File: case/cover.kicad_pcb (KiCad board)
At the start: 2 copper layers, 20.5 x 37 mm, 2 parts

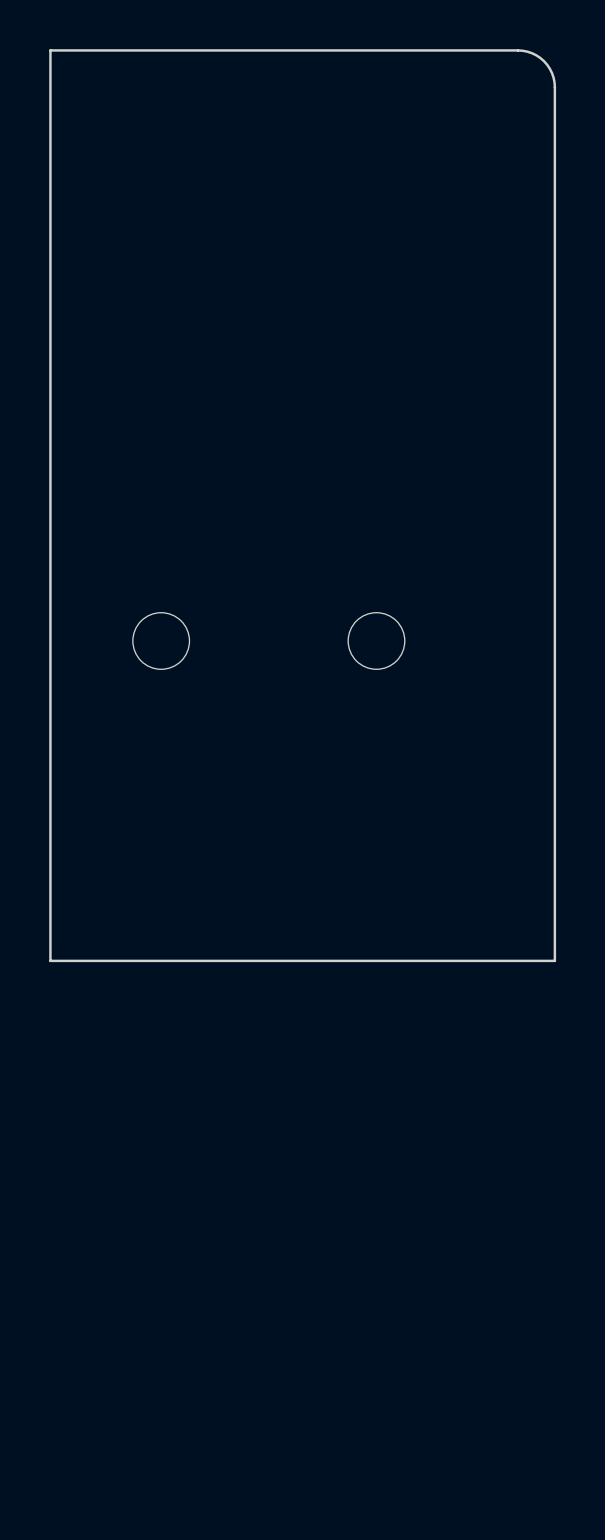
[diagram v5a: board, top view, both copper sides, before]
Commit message: remove small cover
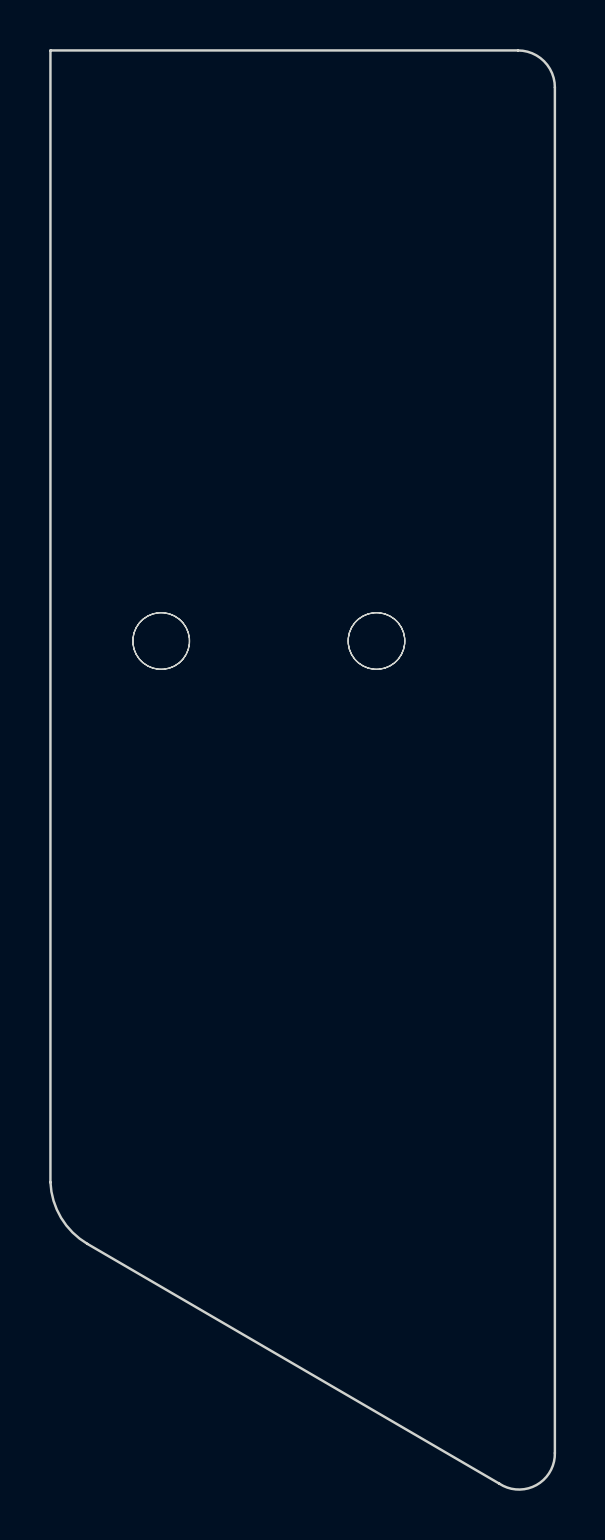
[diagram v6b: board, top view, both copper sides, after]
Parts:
- added H6: MountingHole, kbd:thread_m2, F.Cu at (130.0, 84.0)
- added H7: MountingHole, kbd:thread_m2, F.Cu at (138.8, 84.0)
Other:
- board size 20.5 x 37 mm -> 20.5 x 58.5 mm
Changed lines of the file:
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@@
+    (descr "Mounting Hole 2.2mm, no annular, M2")
+    (tags "mounting hole 2.2mm no annular m2")
+    (property "Sheetfile" "full.kicad_sch")
+    (property "Sheetname" "")
+    (attr exclude_from_pos_files)
+    (fp_text reference "H6" (at -0.95 -0.55) (layer "F.Fab") hide
+      (effects (font (size 1 1) (thickness 0.15)))
+    )
+    (fp_text value "MountingHole" (at 0 0.55) (layer "F.Fab") hide
+      (effects (font (size 1 1) (thickness 0.15)))
+    )
+    (pad "" np_thru_hole circle locked (at 0 0) (size 2.3 2.3) (drill 2.3) (layers *.Cu *.Mask))
+  )
+  (footprint "kbd:thread_m2" (layer "F.Cu")
+    (at 138.75 84)
+    (descr "Mounting Hole 2.2mm, no annular, M2")
+    (tags "mounting hole 2.2mm no annular m2")
+    (property "Sheetfile" "full.kicad_sch")
+    (property "Sheetname" "")
+    (attr exclude_from_pos_files)
+    (fp_text reference "H7" (at -0.95 -0.55) (layer "F.Fab") hide
+      (effects (font (size 1 1) (thickness 0.15)))
+    )
+    (fp_text value "MountingHole" (at 0 0.55) (layer "F.Fab") hide
+      (effects (font (size 1 1) (thickness 0.15)))
+    )
+    (pad "" np_thru_hole circle locked (at 0 0) (size 2.3 2.3) (drill 2.3) (layers *.Cu *.Mask))
+  )
+  (footprint "kbd:thread_m2" (layer "F.Cu")
+    (at 130 84)
     (descr "Mounting Hole 2.2mm, no annular, M2")
     (tags "mounting hole 2.2mm no annular m2")
@@
     (pad "" np_thru_hole circle locked (at 0 0) (size 2.3 2.3) (drill 2.3) (layers *.Cu *.Mask))
   )
-  (gr_line (start 125.5 97) (end 125.5 60) (layer "Edge.Cuts") (width 0.1))
+  (gr_line (start 125.5 106) (end 125.5 60) (layer "Edge.Cuts") (width 0.1))
   (gr_arc (start 144.5 60) (mid 145.56066 60.43934) (end 146 61.5) (layer "Edge.Cuts") (width 0.1))
-  (gr_line (start 146 97) (end 146 61.5) (layer "Edge.Cuts") (width 0.1))
-  (gr_line (start 146 97) (end 125.5 97) (layer "Edge.Cuts") (width 0.1))
+  (gr_line (start 127 108.5) (end 143.75 118.25) (layer "Edge.Cuts") (width 0.1))
+  (gr_arc (start 127 108.5) (mid 125.931823 107.440906) (end 125.5 106) (layer "Edge.Cuts") (width 0.1))
+  (gr_line (start 146 117) (end 146 61.5) (layer "Edge.Cuts") (width 0.1))
+  (gr_arc (start 146 117) (mid 145.251202 118.302163) (end 143.75 118.25) (layer "Edge.Cuts") (width 0.1))
   (gr_line (start 144.5 60) (end 125.5 60) (layer "Edge.Cuts") (width 0.1))
 )

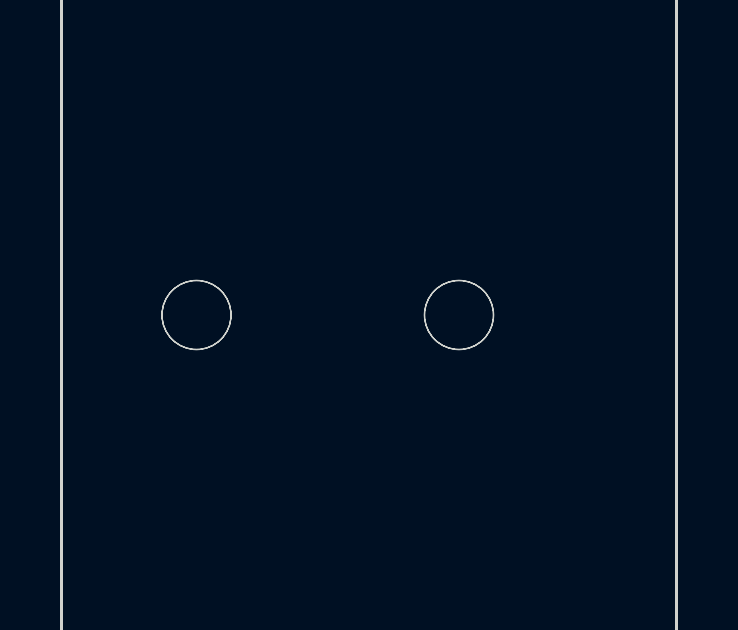
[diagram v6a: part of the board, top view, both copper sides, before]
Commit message: fix dxf files
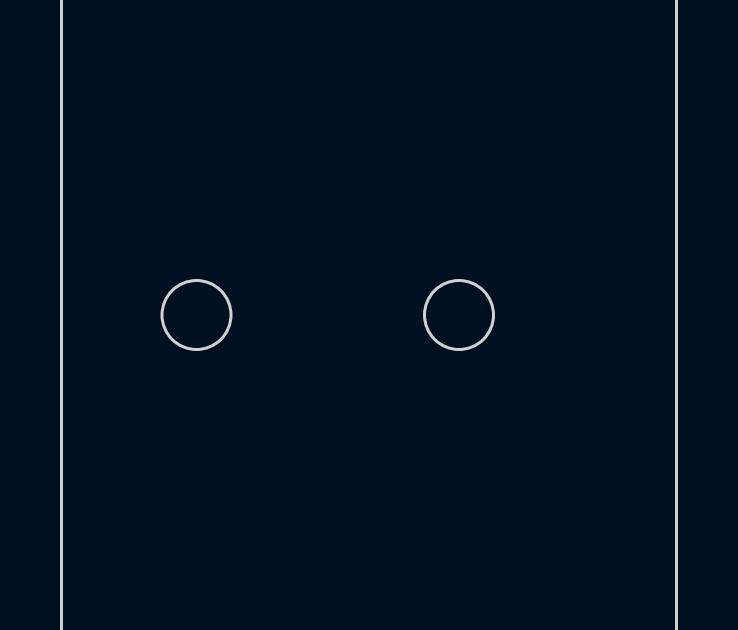
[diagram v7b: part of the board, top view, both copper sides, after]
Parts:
- removed the H6 at (130.0, 84.0)
- removed the H7 at (138.8, 84.0)
- H6, H7: footprint kbd:thread_m2 -> pica:thread_m2_hole
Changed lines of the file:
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@@
     (pad_to_mask_clearance 0)
     (pcbplotparams
-      (layerselection 0x0000080_7ffffffe)
+      (layerselection 0x0001000_7ffffffe)
       (disableapertmacros false)
       (usegerberextensions true)
@@
       (svguseinch false)
       (svgprecision 6)
-      (excludeedgelayer false)
+      (excludeedgelayer true)
       (plotframeref false)
       (viasonmask false)
@@
       (hpglpenspeed 20)
       (hpglpendiameter 15.000000)
-      (dxfpolygonmode true)
+      (dxfpolygonmode false)
       (dxfimperialunits false)
       (dxfusepcbnewfont true)
@@
   )
   (net 0 "")
-  (footprint "kbd:thread_m2" (layer "F.Cu")
+  (footprint "pica:thread_m2_hole" (layer "F.Cu")
     (at 138.75 84)
     (descr "Mounting Hole 2.2mm, no annular, M2")
     (tags "mounting hole 2.2mm no annular m2")
-    (property "Sheetfile" "left.kicad_sch")
+    (property "Sheetfile" "full.kicad_sch")
     (property "Sheetname" "")
-    (attr exclude_from_pos_files)
+    (attr exclude_from_pos_files exclude_from_bom)
     (fp_text reference "H7" (at -0.95 -0.55) (layer "F.Fab") hide
       (effects (font (size 1 1) (thickness 0.15)))
@@
       (effects (font (size 1 1) (thickness 0.15)))
     )
-    (pad "" np_thru_hole circle locked (at 0 0) (size 2.3 2.3) (drill 2.3) (layers *.Cu *.Mask))
+    (fp_circle (center 0 0) (end 1.15 0) (layer "Edge.Cuts") (width 0.1) (fill none))
   )
-  (footprint "kbd:thread_m2" (layer "F.Cu")
+  (footprint "pica:thread_m2_hole" (layer "F.Cu")
     (at 130 84)
     (descr "Mounting Hole 2.2mm, no annular, M2")
     (tags "mounting hole 2.2mm no annular m2")
-    (property "Sheetfile" "full.kicad_sch")
+    (property "Sheetfile" "left.kicad_sch")
     (property "Sheetname" "")
-    (attr exclude_from_pos_files)
+    (attr exclude_from_pos_files exclude_from_bom)
     (fp_text reference "H6" (at -0.95 -0.55) (layer "F.Fab") hide
       (effects (font (size 1 1) (thickness 0.15)))
@@
       (effects (font (size 1 1) (thickness 0.15)))
     )
-    (pad "" np_thru_hole circle locked (at 0 0) (size 2.3 2.3) (drill 2.3) (layers *.Cu *.Mask))
-  )
-  (footprint "kbd:thread_m2" (layer "F.Cu")
-    (at 138.75 84)
-    (descr "Mounting Hole 2.2mm, no annular, M2")
-    (tags "mounting hole 2.2mm no annular m2")
-    (property "Sheetfile" "full.kicad_sch")
-    (property "Sheetname" "")
-    (attr exclude_from_pos_files)
-    (fp_text reference "H7" (at -0.95 -0.55) (layer "F.Fab") hide
-      (effects (font (size 1 1) (thickness 0.15)))
-    )
-    (fp_text value "MountingHole" (at 0 0.55) (layer "F.Fab") hide
-      (effects (font (size 1 1) (thickness 0.15)))
-    )
-    (pad "" np_thru_hole circle locked (at 0 0) (size 2.3 2.3) (drill 2.3) (layers *.Cu *.Mask))
-  )
-  (footprint "kbd:thread_m2" (layer "F.Cu")
-    (at 130 84)
-    (descr "Mounting Hole 2.2mm, no annular, M2")
-    (tags "mounting hole 2.2mm no annular m2")
-    (property "Sheetfile" "left.kicad_sch")
-    (property "Sheetname" "")
-    (attr exclude_from_pos_files)
-    (fp_text reference "H6" (at -0.95 -0.55) (layer "F.Fab") hide
-      (effects (font (size 1 1) (thickness 0.15)))
-    )
-    (fp_text value "MountingHole" (at 0 0.55) (layer "F.Fab") hide
-      (effects (font (size 1 1) (thickness 0.15)))
-    )
-    (pad "" np_thru_hole circle locked (at 0 0) (size 2.3 2.3) (drill 2.3) (layers *.Cu *.Mask))
+    (fp_circle (center 0 0) (end 1.15 0) (layer "Edge.Cuts") (width 0.1) (fill none))
   )
   (gr_line (start 125.5 106) (end 125.5 60) (layer "Edge.Cuts") (width 0.1))
